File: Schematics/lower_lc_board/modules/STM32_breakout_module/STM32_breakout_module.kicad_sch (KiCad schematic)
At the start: 42 parts, among them J2 SWD_CONN, J3 USB_C_CONN, SW1 SW_STM_RESET, SW2 SW_STM_BOOT_MODE, U5 STM32F103CBT6, U6 W25Q128JVS, U7 ISO1044BDR, U8 CP2102N-Axx-xQFN28, Y1 X322516MMB4SI

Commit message: pin assignments verified
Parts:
- removed TP9: PA9, TestPoint:TestPoint_Pad_1.5x1.5mm, symbol Connector:TestPoint
- added C45: 0.1uF, Capacitor_SMD:C_0805_2012Metric, symbol Device:C
- TP7: value PB6 -> USB-DM; footprint TestPoint:TestPoint_Pad_1.5x1.5mm -> TestPoint:TestPoint_Pad_D1.5mm; now in the parts list
- TP8: value PB7 -> USB-DP; footprint TestPoint:TestPoint_Pad_1.5x1.5mm -> TestPoint:TestPoint_Pad_D1.5mm; now in the parts list
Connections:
- net GPIO_41 is gone; now on net CAN_LED: R15.1
- net GPIO_42 is gone; now on net FAULT_LED: R14.1
- net ADC_CLKIN: now also U5.29 (PA8)
- net GND: now also C45.1
- net HALL_LED: now also U5.14 (PA4)
- net HALL_SCL: now also U5.42 (PB6)
- net HALL_SDA: now also U5.43 (PB7)
- net PT_LED: now also U5.12 (PA2)
- net RESET_FL: now also U5.25 (PB12); no longer U5.29 (PA8)
- net TC_LED: now also U5.13 (PA3)
- net TEMP_SENSE: now also U5.17 (PA7), C45.2
- net VALVE1_CTRL: now also U5.10 (PA0)
- net VALVE2_CTRL: now also U5.11 (PA1)
- net at TP7.1: now also U5.32 (PA11); no longer U5.42 (PB6)
- net FAULT_LED: now reaches U5.30 (PA9)
- net at TP8.1: now also U5.33 (PA12); no longer U5.43 (PB7)
- net FL_CS: now reaches U5.15 (PA5)
- net FL_CS: now also U6.1 (~{CS})
- net ADC_CS: now reaches U5.16 (PA6)
- net CAN_LED: now reaches U5.19 (PB1)
- net ADC_DRDY: now reaches U5.31 (PA10)
- removed net CS_FL: U5.25 (PB12), U6.1 (~{CS})
- net MISO_FL renamed MISO
- net MOSI_FL renamed MOSI
- net SCK_FL renamed SCK
- net USB_RX renamed USART-TX
- net USART-TX: no longer U8.26 (TXD)
- net USB_TX renamed USART-RX
- net USART-RX: no longer U8.25 (RXD)
- new net USART_RX: U8.26 (TXD)
- new net USART_TX: U8.25 (RXD)
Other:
- note added: "* needs software remap"
- note added: "place near PA7 to filter switching noise from adjacent MCO pin"
- note added: "usb DM/DP"
- note removed: "IO Label Mappings"

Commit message: start layout
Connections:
- net ADC_CLKIN: now also U5.11 (PA1); no longer U5.29 (PA8)
- net ADC_CS: now also U5.13 (PA3); no longer U5.16 (PA6)
- net ADC_DRDY: now also U5.10 (PA0); no longer U5.31 (PA10)
- net FL_CS: now also U5.12 (PA2); no longer U5.15 (PA5)
- net HALL_LED: no longer U5.14 (PA4)
- net PT_LED: no longer U5.12 (PA2)
- net TC_LED: no longer U5.13 (PA3)
- net TEMP_SENSE: now also U5.14 (PA4); no longer U5.17 (PA7)
- net VALVE1_CTRL: now also U5.29 (PA8); no longer U5.10 (PA0)
- net VALVE2_CTRL: now also U5.31 (PA10); no longer U5.11 (PA1)
- net MISO renamed FL_MISO
- net MOSI renamed FL_MOSI
- net SCK renamed FL_SCK
- new net ADC_MISO: U5.16 (PA6)
- new net ADC_MOSI: U5.17 (PA7)
- new net ADC_SCLK: U5.15 (PA5)

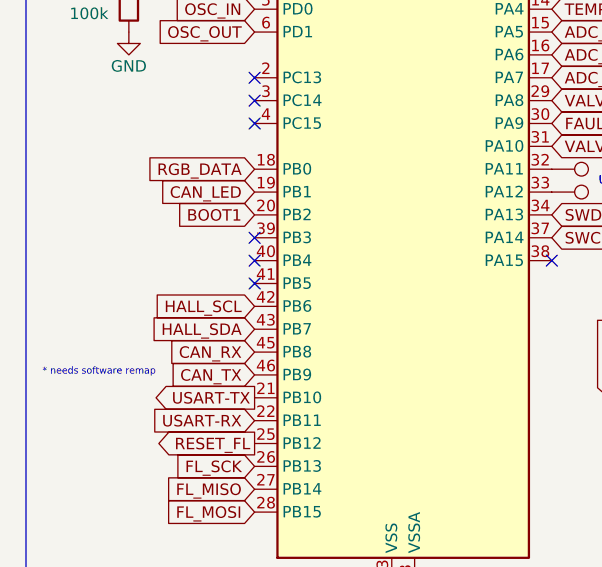
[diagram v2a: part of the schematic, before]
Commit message: replace sensing LEDs with a single
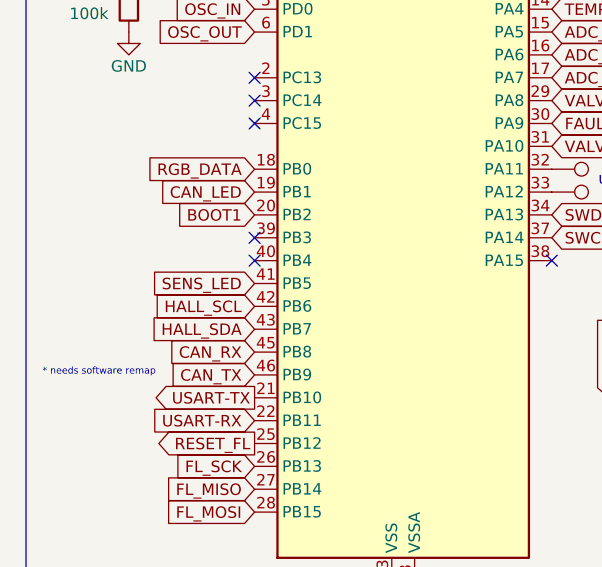
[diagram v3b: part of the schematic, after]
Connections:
- net SENS_LED: now reaches U5.41 (PB5)
- no-connect marks 28 -> 27
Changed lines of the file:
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@@
-	)
-	(no_connect
-		(at 41.91 88.9)
 	)
 	(no_connect
@@
 			(effects
 				(font
+					(size 1.27 1.27)
+				)
+				(justify right)
+				(hide yes)
+			)
+		)
+	)
+	(global_label "SENS_LED"
+		(shape input)
+		(at 41.91 88.9 180)
+		(fields_autoplaced yes)
+		(effects
+			(font
+				(size 1.27 1.27)
+			)
+			(justify right)
+		)
+		(property "Intersheetrefs" "${INTERSHEET_REFS}"
+			(at 29.6116 88.9 0)
+			(effects
+				(font

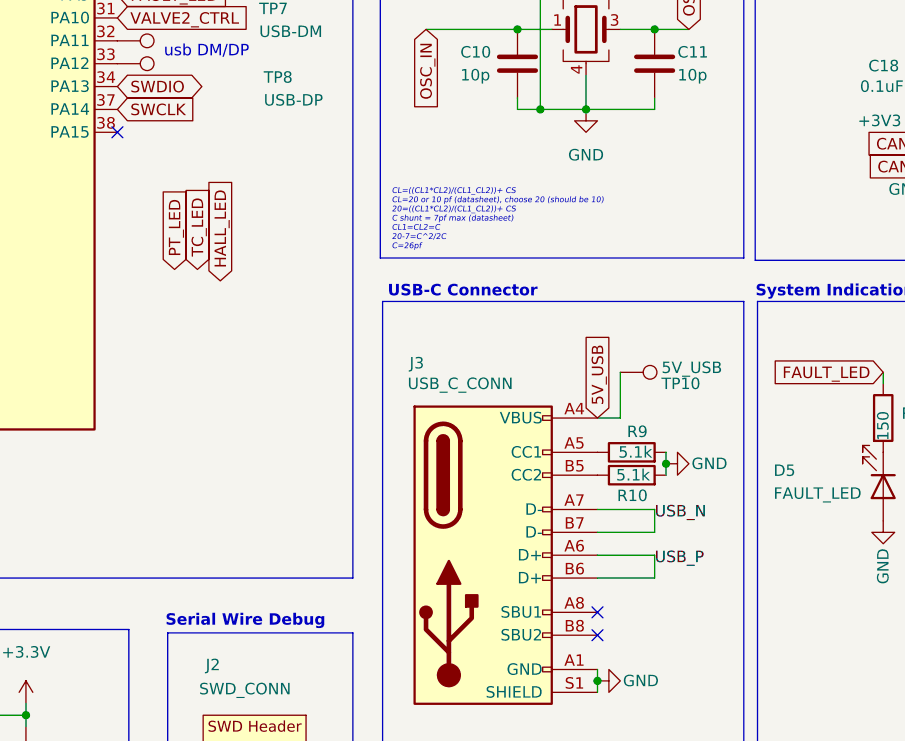
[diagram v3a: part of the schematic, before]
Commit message: layout work
#TODO
- smaller 3V3 buck, add HF cap
- finish layout
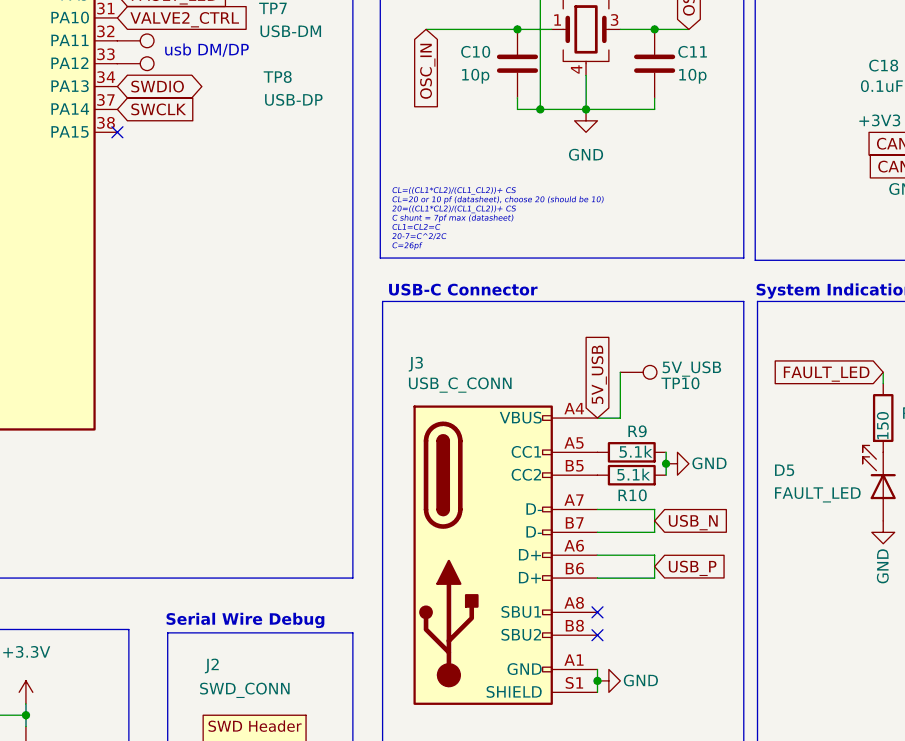
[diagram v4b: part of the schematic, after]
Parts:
- SW1: footprint Button_Switch_SMD:SW_Push_1P1T_XKB_TS-1187A -> TestPoint:TestPoint_Pad_1.0x1.0mm
- TP7, TP8: footprint TestPoint:TestPoint_Pad_D1.5mm -> TestPoint:TestPoint_Pad_1.0x1.0mm
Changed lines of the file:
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@@
 		)
 	)
-	(label "USB_N"
-		(at 134.62 129.54 0)
-		(fields_autoplaced yes)
-		(effects
-			(font
-				(size 1.27 1.27)
-				(color 0 0 0 1)
-			)
-			(justify left bottom)
-		)
-	)
-	(label "USB_P"
-		(at 134.62 134.62 0)
-		(fields_autoplaced yes)
-		(effects
-			(font
-				(size 1.27 1.27)
-				(color 0 0 0 1)
-			)
-			(justify left bottom)
-		)
-	)
 	(global_label "OSC_IN"
 		(shape input)
@@
 		)
 	)
-	(global_label "FL_CS"
+	(global_label "USB_P"
 		(shape input)
-		(at 173.99 40.64 180)
+		(at 134.62 134.62 0)
 		(fields_autoplaced yes)
 		(effects
@@
 				(size 1.27 1.27)
 			)
-			(justify right)
+			(justify left)
 		)
 		(property "Intersheetrefs" "${INTERSHEET_REFS}"
-			(at 165.441 40.64 0)
+			(at 143.6528 134.62 0)
 			(effects
 				(font
 					(size 1.27 1.27)
 				)
-				(justify right)
+				(justify left)
 				(hide yes)
 			)
 		)
 	)
-	(global_label "5V_USB"
+	(global_label "FL_CS"
 		(shape input)
-		(at 128.27 118.11 90)
+		(at 173.99 40.64 180)
 		(fields_autoplaced yes)
 		(effects
@@
 				(size 1.27 1.27)
 			)
-			(justify left)
+			(justify right)
 		)
 		(property "Intersheetrefs" "${INTERSHEET_REFS}"
-			(at 128.27 108.0491 90)
+			(at 165.441 40.64 0)
 			(effects
 				(font
 					(size 1.27 1.27)
 				)
-				(justify left)
+				(justify right)
 				(hide yes)
 			)
 		)
 	)
-	(global_label "VALVE1_CTRL"
+	(global_label "5V_USB"
 		(shape input)
-		(at 74.93 68.58 0)
+		(at 128.27 118.11 90)
 		(fields_autoplaced yes)
 		(effects
@@
 		)
 		(property "Intersheetrefs" "${INTERSHEET_REFS}"
-			(at 90.0709 68.58 0)
+			(at 128.27 108.0491 90)
 			(effects
 				(font
@@
 		)
 	)
-	(global_label "STM_RESET"
-		(shape output)
-		(at 121.92 48.26 0)
+	(global_label "VALVE1_CTRL"
+		(shape input)
+		(at 74.93 68.58 0)
 		(fields_autoplaced yes)
 		(effects
@@
 		)
 		(property "Intersheetrefs" "${INTERSHEET_REFS}"
-			(at 135.2464 48.26 0)
+			(at 90.0709 68.58 0)
 			(effects
 				(font
@@
 		)
 	)
-	(global_label "PT_LED"
-		(shape input)
-		(at 81.28 101.6 90)
+	(global_label "STM_RESET"
+		(shape output)
+		(at 121.92 48.26 0)
 		(fields_autoplaced yes)
 		(effects
@@
 		)
 		(property "Intersheetrefs" "${INTERSHEET_REFS}"
-			(at 81.28 91.9625 90)
+			(at 135.2464 48.26 0)
 			(effects
 				(font
@@
 		)
 	)
-	(global_label "ADC_CLKIN"
+	(global_label "USB_N"
 		(shape input)
-		(at 74.93 50.8 0)
+		(at 134.62 129.54 0)
 		(fields_autoplaced yes)
 		(effects
@@
 		)
 		(property "Intersheetrefs" "${INTERSHEET_REFS}"
-			(at 88.0148 50.8 0)
+			(at 143.7133 129.54 0)
 			(effects
 				(font
@@
 		)
 	)
-	(global_label "RGB_DATA"
+	(global_label "ADC_CLKIN"
 		(shape input)
-		(at 41.91 76.2 180)
+		(at 74.93 50.8 0)
 		(fields_autoplaced yes)
 		(effects
@@
 				(size 1.27 1.27)
 			)
-			(justify right)
+			(justify left)
 		)
 		(property "Intersheetrefs" "${INTERSHEET_REFS}"
-			(at 29.7324 76.2 0)
+			(at 88.0148 50.8 0)
 			(effects
 				(font
 					(size 1.27 1.27)
 				)
-				(justify right)
+				(justify left)
 				(hide yes)
 			)
 		)
 	)
-	(global_label "HALL_LED"
+	(global_label "RGB_DATA"
 		(shape input)
-		(at 86.36 102.87 90)
+		(at 41.91 76.2 180)
 		(fields_autoplaced yes)
 		(effects
@@
 				(size 1.27 1.27)
 			)
-			(justify left)
+			(justify right)
 		)
 		(property "Intersheetrefs" "${INTERSHEET_REFS}"
-			(at 86.36 90.9948 90)
+			(at 29.7324 76.2 0)
 			(effects
 				(font
 					(size 1.27 1.27)
 				)
-				(justify left)
+				(justify right)
 				(hide yes)
 			)
@@
 		)
 	)
-	(global_label "TC_LED"
-		(shape input)
-		(at 83.82 101.6 90)
-		(fields_autoplaced yes)
-		(effects
-			(font
-				(size 1.27 1.27)
-			)
-			(justify left)
-		)
-		(property "Intersheetrefs" "${INTERSHEET_REFS}"
-			(at 83.82 91.9625 90)
-			(effects
-				(font
-					(size 1.27 1.27)
-				)
-				(justify left)
-				(hide yes)
-			)
-		)
-	)
 	(symbol
 		(lib_id "power:GND")
@@
 			)
 		)
-		(property "Footprint" "Button_Switch_SMD:SW_Push_1P1T_XKB_TS-1187A"
+		(property "Footprint" "TestPoint:TestPoint_Pad_1.0x1.0mm"
 			(at 116.84 43.18 0)
 			(effects
@@
 			)
 		)
-		(property "Footprint" "TestPoint:TestPoint_Pad_D1.5mm"
+		(property "Footprint" "TestPoint:TestPoint_Pad_1.0x1.0mm"
 			(at 74.93 81.28 0)
 			(effects
@@
 			)
 		)
-		(property "Footprint" "TestPoint:TestPoint_Pad_D1.5mm"
+		(property "Footprint" "TestPoint:TestPoint_Pad_1.0x1.0mm"
 			(at 74.93 83.82 0)
 			(effects

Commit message: layout work
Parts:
- SW1: footprint TestPoint:TestPoint_Pad_1.0x1.0mm -> Button_Switch_SMD:SW_Push_1P1T_XKB_TS-1187A
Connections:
- net USART-RX is gone; now on net USART_RX: U5.22 (PB11)
- net USART-TX is gone; now on net USART_TX: U5.21 (PB10)
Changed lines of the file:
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@@
 		)
 	)
-	(global_label "USART-RX"
+	(global_label "USART_RX"
 		(shape input)
 		(at 41.91 104.14 180)
@@
 		)
 		(property "Intersheetrefs" "${INTERSHEET_REFS}"
-			(at 29.0067 104.14 0)
+			(at 29.6115 104.14 0)
 			(effects
 				(font
@@
 		)
 	)
-	(global_label "USART-TX"
+	(global_label "USART_TX"
 		(shape output)
 		(at 41.91 101.6 180)
@@
 		)
 		(property "Intersheetrefs" "${INTERSHEET_REFS}"
-			(at 29.3091 101.6 0)
+			(at 29.9139 101.6 0)
 			(effects
 				(font
@@
 			)
 		)
-		(property "Footprint" "TestPoint:TestPoint_Pad_1.0x1.0mm"
+		(property "Footprint" "Button_Switch_SMD:SW_Push_1P1T_XKB_TS-1187A"
 			(at 116.84 43.18 0)
 			(effects

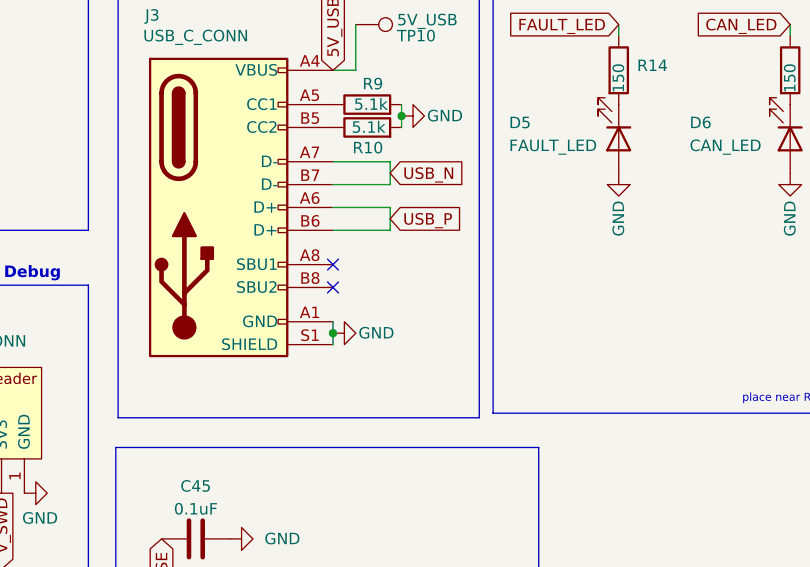
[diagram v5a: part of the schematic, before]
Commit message: add power switching for PTs (schematic only)
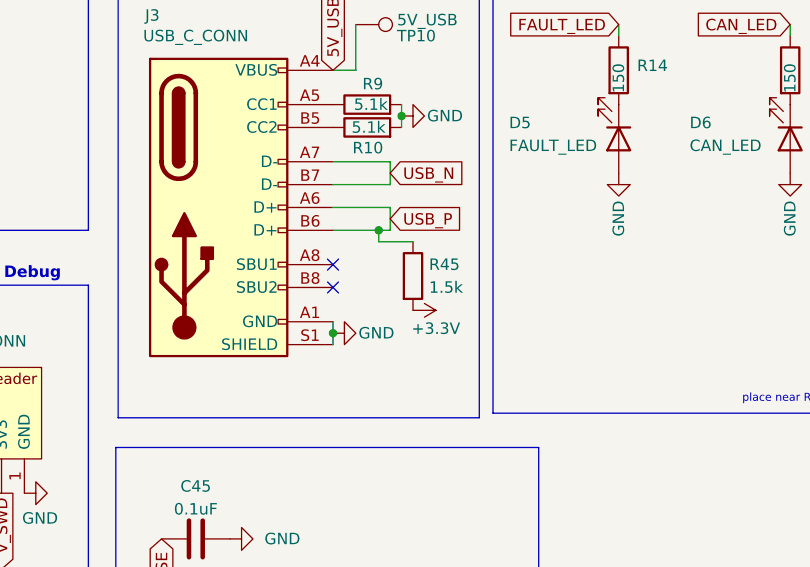
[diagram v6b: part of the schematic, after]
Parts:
- added R45: 1.5k, Resistor_SMD:R_0402_1005Metric, symbol Device:R
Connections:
- net +3.3V: now also R45.2
- net USB_P: now also R45.1
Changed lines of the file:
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@@
 	)
 	(junction
+		(at 133.35 135.89)
+		(diameter 0)
+		(color 0 0 0 0)
+	)
+	(junction
 		(at 34.29 158.75)
 		(diameter 0)
@@
 	(wire
 		(pts
+			(xy 133.35 135.89) (xy 133.35 137.16)
+		)
+		(stroke
+			(width 0)
+			(type default)
+			(color 47 120 160 1)
+		)
+	)
+	(wire
+		(pts
+			(xy 133.35 137.16) (xy 137.16 137.16)
+		)
+		(stroke
+			(width 0)
+			(type default)
+			(color 47 120 160 1)
+		)
+	)
+	(wire
+		(pts
 			(xy 149.86 56.515) (xy 173.99 56.515)
 		)
@@
 	(wire
 		(pts
-			(xy 128.27 135.89) (xy 134.62 135.89)
+			(xy 128.27 135.89) (xy 133.35 135.89)
 		)
 		(stroke
@@
 	(wire
 		(pts
+			(xy 133.35 135.89) (xy 134.62 135.89)
+		)
+		(stroke
+			(width 0)
+			(type default)
+			(color 47 120 160 1)
+		)
+	)
+	(wire
+		(pts
 			(xy 149.86 50.8) (xy 149.86 56.515)
 		)
@@
 	)
 	(symbol
+		(lib_id "Device:R")
+		(at 137.16 140.97 0)
+		(unit 1)
+		(exclude_from_sim no)
+		(in_bom yes)
+		(on_board yes)
+		(dnp no)
+		(property "Reference" "R45"
+			(at 138.938 139.7 0)
+			(effects
+				(font
+					(size 1.27 1.27)
+				)
+				(justify left)
+			)
+		)
+		(property "Value" "1.5k"
+			(at 138.938 142.24 0)
+			(effects
+				(font
+					(size 1.27 1.27)
+				)
+				(justify left)
+			)
+		)
+		(property "Footprint" "Resistor_SMD:R_0402_1005Metric"
+			(at 135.382 140.97 90)
+			(effects
+				(font
+					(size 1.27 1.27)
+				)
+				(hide yes)
+			)
+		)
+		(property "Datasheet" "~"
+			(at 137.16 140.97 0)
+			(effects
+				(font
+					(size 1.27 1.27)
+				)
+				(hide yes)
+			)
+		)
+		(property "Description" "Resistor"
+			(at 137.16 140.97 0)
+			(effects
+				(font
+					(size 1.27 1.27)
+				)
+				(hide yes)
+			)
+		)
+		(pin "1"
+		)
+		(pin "2"
+		)
+		(instances
+			(project ""
+				(path "/d63798c4-e363-437e-9012-e4aff32e6642/925ef91a-c900-4b94-a159-606c279d7192"
+					(reference "R45")
+					(unit 1)
+				)
+			)
+		)
+	)
+	(symbol
 		(lib_id "Connector:TestPoint")
 		(at 74.93 78.74 270)
@@
 					(unit 1)
 				)
+			)
+		)
+	)
+	(symbol
+		(lib_id "power:+3.3V")
+		(at 137.16 144.78 270)
+		(unit 1)
+		(exclude_from_sim no)
+		(in_bom yes)
+		(on_board yes)
+		(dnp no)
+		(property "Reference" "#PWR0111"
+			(at 133.35 144.78 0)
+			(effects
+				(font
+					(size 1.27 1.27)
+				)
+				(hide yes)
+			)
+		)
+		(property "Value" "+3.3V"
+			(at 139.7 146.812 90)
+			(effects
+				(font
+					(size 1.27 1.27)
+				)
+			)
+		)
+		(property "Footprint" ""
+			(at 137.16 144.78 0)
+			(effects
+				(font
+					(size 1.27 1.27)
+				)
+				(hide yes)
+			)
+		)
+		(property "Datasheet" ""
+			(at 137.16 144.78 0)
+			(effects
+				(font
+					(size 1.27 1.27)
+				)
+				(hide yes)
+			)
+		)
+		(property "Description" ""
+			(at 137.16 144.78 0)
+			(effects
+				(font
+					(size 1.27 1.27)
+				)
+				(hide yes)
+			)
+		)
+		(pin "1"
+		)
+		(instances
+			(project "lower_lc_board"
+				(path "/d63798c4-e363-437e-9012-e4aff32e6642/925ef91a-c900-4b94-a159-606c279d7192"
+					(reference "#PWR0111")
+					(unit 1)
+				)

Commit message: more layout work, add testing code
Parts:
- added BZ1: Buzzer, symbol Device:Buzzer
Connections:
- net SENS_LED is gone; now on net CAN_LED: U5.41 (PB5)
- net CAN_LED: no longer U5.19 (PB1)
- new net VPT-SW: U5.19 (PB1)
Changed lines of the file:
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@@
 		)
 	)
-	(global_label "CAN_LED"
+	(global_label "FL_MISO"
 		(shape input)
-		(at 41.91 78.74 180)
+		(at 173.99 48.26 180)
 		(fields_autoplaced yes)
 		(effects
@@
 		)
 		(property "Intersheetrefs" "${INTERSHEET_REFS}"
-			(at 30.821 78.74 0)
+			(at 163.3243 48.26 0)
 			(effects
 				(font
@@
 		)
 	)
-	(global_label "FL_MISO"
+	(global_label "CAN_H"
 		(shape input)
-		(at 173.99 48.26 180)
+		(at 187.96 87.63 0)
 		(fields_autoplaced yes)
 		(effects
@@
 				(size 1.27 1.27)
 			)
-			(justify right)
+			(justify left)
 		)
 		(property "Intersheetrefs" "${INTERSHEET_REFS}"
-			(at 163.3243 48.26 0)
+			(at 196.9324 87.63 0)
 			(effects
 				(font
 					(size 1.27 1.27)
 				)
-				(justify right)
+				(justify left)
 				(hide yes)
 			)
 		)
 	)
-	(global_label "CAN_H"
+	(global_label "CAN_RX"
 		(shape input)
-		(at 187.96 87.63 0)
+		(at 167.64 87.63 180)
 		(fields_autoplaced yes)
 		(effects
@@
 				(size 1.27 1.27)
 			)
-			(justify left)
+			(justify right)
 		)
 		(property "Intersheetrefs" "${INTERSHEET_REFS}"
-			(at 196.9324 87.63 0)
+			(at 157.5186 87.63 0)
 			(effects
 				(font
 					(size 1.27 1.27)
 				)
-				(justify left)
+				(justify right)
 				(hide yes)
 			)
 		)
 	)
-	(global_label "CAN_RX"
+	(global_label "VPT-SW"
 		(shape input)
-		(at 167.64 87.63 180)
+		(at 41.91 78.74 180)
 		(fields_autoplaced yes)
 		(effects
@@
 		)
 		(property "Intersheetrefs" "${INTERSHEET_REFS}"
-			(at 157.5186 87.63 0)
+			(at 31.3653 78.74 0)
 			(effects
 				(font
@@
 		)
 	)
-	(global_label "ADC_MOSI"
+	(global_label "CAN_LED"
 		(shape input)
-		(at 74.93 66.04 0)
+		(at 41.91 88.9 180)
 		(fields_autoplaced yes)
 		(effects
@@
 				(size 1.27 1.27)
 			)
-			(justify left)
+			(justify right)
 		)
 		(property "Intersheetrefs" "${INTERSHEET_REFS}"
-			(at 87.1076 66.04 0)
+			(at 30.821 88.9 0)
 			(effects
 				(font
 					(size 1.27 1.27)
 				)
-				(justify left)
+				(justify right)
 				(hide yes)
 			)
 		)
 	)
-	(global_label "FL_MISO"
+	(global_label "ADC_MOSI"
 		(shape input)
-		(at 41.91 111.76 180)
+		(at 74.93 66.04 0)
 		(fields_autoplaced yes)
 		(effects
@@
 				(size 1.27 1.27)
 			)
-			(justify right)
+			(justify left)
 		)
 		(property "Intersheetrefs" "${INTERSHEET_REFS}"
-			(at 31.2443 111.76 0)
+			(at 87.1076 66.04 0)
 			(effects
 				(font
 					(size 1.27 1.27)
 				)
-				(justify right)
+				(justify left)
 				(hide yes)
 			)
 		)
 	)
-	(global_label "RESET_FL"
-		(shape output)
-		(at 41.91 106.68 180)
+	(global_label "FL_MISO"
+		(shape input)
+		(at 41.91 111.76 180)
 		(fields_autoplaced yes)
 		(effects
@@
 		)
 		(property "Intersheetrefs" "${INTERSHEET_REFS}"
-			(at 30.0954 106.68 0)
+			(at 31.2443 111.76 0)
 			(effects
 				(font
@@
 		)
 	)
-	(global_label "SENS_LED"
-		(shape input)
-		(at 41.91 88.9 180)
+	(global_label "RESET_FL"
+		(shape output)
+		(at 41.91 106.68 180)
 		(fields_autoplaced yes)
 		(effects
@@
 		)
 		(property "Intersheetrefs" "${INTERSHEET_REFS}"
-			(at 29.6116 88.9 0)
+			(at 30.0954 106.68 0)
 			(effects
 				(font
@@
 					(unit 1)
 				)
+			)
+		)
+	)
+	(symbol
+		(lib_id "Device:Buzzer")
+		(at 252.73 138.43 0)
+		(unit 1)
+		(exclude_from_sim no)
+		(in_bom yes)
+		(on_board yes)
+		(dnp no)
+		(fields_autoplaced yes)
+		(property "Reference" "BZ1"
+			(at 256.54 137.1599 0)
+			(effects
+				(font
+					(size 1.27 1.27)
+				)
+				(justify left)
+			)
+		)
+		(property "Value" "Buzzer"
+			(at 256.54 139.6999 0)
+			(effects
+				(font
+					(size 1.27 1.27)
+				)
+				(justify left)
+			)
+		)
+		(property "Footprint" ""
+			(at 252.095 135.89 90)
+			(effects
+				(font
+					(size 1.27 1.27)
+				)
+				(hide yes)
+			)
+		)
+		(property "Datasheet" "~"
+			(at 252.095 135.89 90)
+			(effects
+				(font
+					(size 1.27 1.27)
+				)
+				(hide yes)
+			)
+		)
+		(property "Description" "Buzzer, polarized"
+			(at 252.73 138.43 0)
+			(effects
+				(font
+					(size 1.27 1.27)
+				)
+				(hide yes)
+			)
+		)
+		(pin "1"
+		)
+		(pin "2"
+		)
+		(instances
+			(project ""
+				(path "/d63798c4-e363-437e-9012-e4aff32e6642/925ef91a-c900-4b94-a159-606c279d7192"
+					(reference "BZ1")
+					(unit 1)
+				)
